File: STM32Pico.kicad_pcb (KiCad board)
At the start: 2 copper layers, 21.1 x 51.3 mm, 25 parts, among them J1 2.54mm header 01x20, J2 2.54mm header 01x20, SW1 Boot Mode, SW2 Reset Switch, U1 STM32F411CEUx, U2 XC6206PxxxMR, X1 ECS-2520MV-xxx-xx

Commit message: worked on the PCB a bit more, added some zones. yet to assign pins to GPIOs
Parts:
- moved R1 40.5 mm to (104.9, 66.9), turned to 90 degrees
- moved C1 30.8 mm to (109.7, 80.1), turned to 180 degrees
- moved C7 28.0 mm to (108.3, 78.5), turned to 270 degrees
- moved C5 26.1 mm to (98.7, 85.2), turned to 45 degrees
- moved C4 22.8 mm to (99.0, 77.9), turned to 270 degrees
- moved R2 19.4 mm to (101.5, 67.4), turned to 90 degrees
- turned D1 to 90 degrees
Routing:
- net D+: track 0.00 -> 11.3 mm, vias 0 -> 2
- net D-: track 0.00 -> 11.1 mm, vias 0 -> 2
- net +3V3: track 2.95 -> 7.47 mm, vias 3 -> 5
- net GND: track 0.00 -> 3.75 mm, vias 0 -> 1
- net Net-(C1-Pad2): track 0.00 -> 2.17 mm
- net Net-(R2-Pad2): track 0.00 -> 2.12 mm
- net Net-(R1-Pad2): track 0.00 -> 1.47 mm
- added copper zone on F.Cu, net +3V3

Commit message: finished up board design, likely needs some check overs and revision.
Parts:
- moved C2 31.4 mm to (105.5, 87.0)
- moved R6 31.1 mm to (101.8, 91.2), turned to 180 degrees
- moved R7 28.8 mm to (97.6, 92.2), turned to 180 degrees
- moved C3 19.0 mm to (100.0, 72.4)
- moved C9 3.70 mm to (103.6, 86.8), turned to 180 degrees
- moved C4 1.38 mm to (100.2, 77.2), turned to 180 degrees
- moved SW2 1.00 mm to (105.5, 90.5)
- moved C1 0.99 mm to (108.7, 80.0)
- moved X1 0.66 mm to (102.3, 89.0)
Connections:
- J1 pad 1: Net-(J1-Pad1) -> PA2
- J1 pad 10: Net-(J1-Pad10) -> PB8
- J1 pad 11: Net-(J1-Pad11) -> PB7
- J1 pad 12: Net-(J1-Pad12) -> PB6
- J1 pad 14: Net-(J1-Pad14) -> PB5
- J1 pad 15: Net-(J1-Pad15) -> PB4
- J1 pad 16: Net-(J1-Pad16) -> PB3
- J1 pad 17: Net-(J1-Pad17) -> PA15
- J1 pad 19: Net-(J1-Pad19) -> PA14
- J1 pad 2: Net-(J1-Pad2) -> PA1
- J1 pad 20: Net-(J1-Pad20) -> PA13
- J1 pad 4: Net-(J1-Pad4) -> PA0
- J1 pad 5: Net-(J1-Pad5) -> PC15
- J1 pad 6: Net-(J1-Pad6) -> PC14
- J1 pad 7: Net-(J1-Pad7) -> PC13
- J1 pad 9: Net-(J1-Pad9) -> PB9
- J2 pad 10: Net-(J2-Pad10) -> PB15
- J2 pad 11: Net-(J2-Pad11) -> PB14
- J2 pad 12: Net-(J2-Pad12) -> PB13
- J2 pad 14: Net-(J2-Pad14) -> PB12
- J2 pad 15: Net-(J2-Pad15) -> PB10
- J2 pad 16: Net-(J2-Pad16) -> PB2
- J2 pad 17: Net-(J2-Pad17) -> PB1
- J2 pad 19: Net-(J2-Pad19) -> PB0
- J2 pad 20: Net-(J2-Pad20) -> PA7
- J2 pad 6: Net-(J2-Pad6) -> PA10
- J2 pad 7: Net-(J2-Pad7) -> PA9
- J2 pad 9: Net-(J2-Pad9) -> PA8
- U1 pad 10: (no net) -> PA0
- U1 pad 11: (no net) -> PA1
- U1 pad 12: (no net) -> PA2
- U1 pad 17: (no net) -> PA7
- U1 pad 18: (no net) -> PB0
- U1 pad 19: (no net) -> PB1
- U1 pad 2: (no net) -> PC13
- U1 pad 20: (no net) -> PB2
- U1 pad 21: (no net) -> PB10
- U1 pad 23: (no net) -> GND
- U1 pad 25: (no net) -> PB12
- U1 pad 26: (no net) -> PB13
- U1 pad 27: (no net) -> PB14
- U1 pad 28: (no net) -> PB15
- U1 pad 29: (no net) -> PA8
- U1 pad 3: (no net) -> PC14
- U1 pad 30: (no net) -> PA9
- U1 pad 31: (no net) -> PA10
- U1 pad 34: (no net) -> PA13
- U1 pad 35: (no net) -> GND
- U1 pad 37: (no net) -> PA14
- U1 pad 38: (no net) -> PA15
- U1 pad 39: (no net) -> PB3
- U1 pad 4: (no net) -> PC15
- U1 pad 40: (no net) -> PB4
- U1 pad 41: (no net) -> PB5
- U1 pad 42: (no net) -> PB6
- U1 pad 43: (no net) -> PB7
- U1 pad 45: (no net) -> PB8
- U1 pad 46: (no net) -> PB9
- U1 pad 47: (no net) -> GND
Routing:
- net +3V3: track 7.47 -> 45.4 mm, vias 5 -> 8
- net PA7: track 0.00 -> 29.6 mm
- net PA2: track 0.00 -> 28.0 mm
- net PA1: track 0.00 -> 25.9 mm
- net PB0: track 0.00 -> 25.4 mm
- net PA13: track 0.00 -> 24.9 mm
- net PA14: track 0.00 -> 21.5 mm
- net PA0: track 0.00 -> 21.4 mm
- net PB1: track 0.00 -> 20.8 mm
- net PB12: track 0.00 -> 20.4 mm
- net PB2: track 0.00 -> 18.7 mm
- net PB10: track 0.00 -> 16.6 mm
- net PB13: track 0.00 -> 16.3 mm
- net PA15: track 0.00 -> 15.9 mm
- net PB14: track 0.00 -> 14.7 mm
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
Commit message: cleaned up some bits and pieces.
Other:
- board text added: "https://github.com/Envious-Data/STM32Pico"

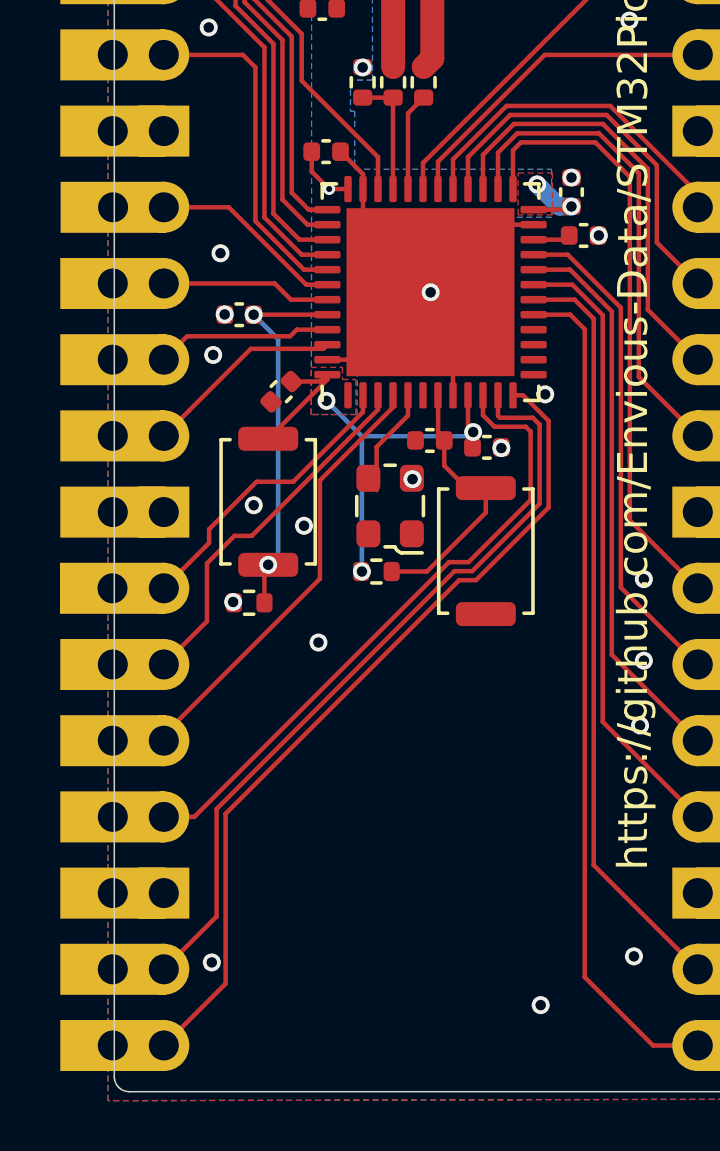
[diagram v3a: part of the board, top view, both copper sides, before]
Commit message: Generated some JLCPCB compatible Gerbers.
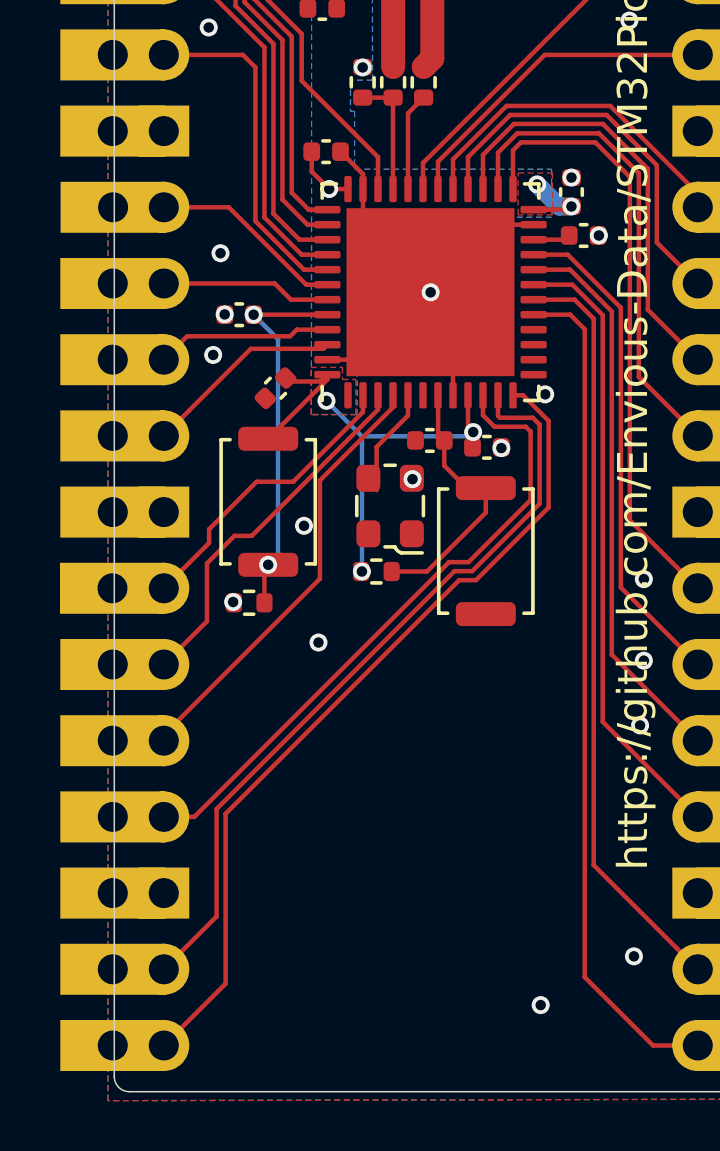
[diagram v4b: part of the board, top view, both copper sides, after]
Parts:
- moved C5 0.22 mm to (98.5, 85.1)
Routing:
- net GND: vias 28 -> 26

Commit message: properly seperated VBUS and VSYS however VSYS is now 5V output only since its not connected to the power management IC
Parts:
- D1: value Schottky 0603 -> 1N4002 0603
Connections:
- D1 pad 1: VBUS -> VSYS
- J2 pad 2: VBUS -> VSYS
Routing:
- added copper zone on F.Cu, net VSYS

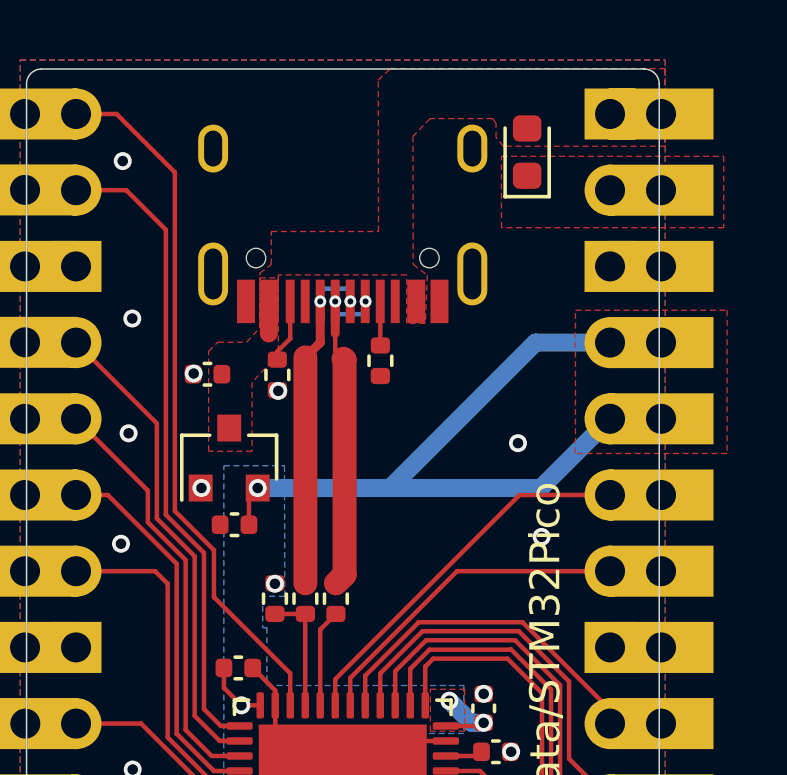
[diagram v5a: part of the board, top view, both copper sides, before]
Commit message: changed my mind - moved power ic to vsys and also adjusted USB traces to correct some phase skew.
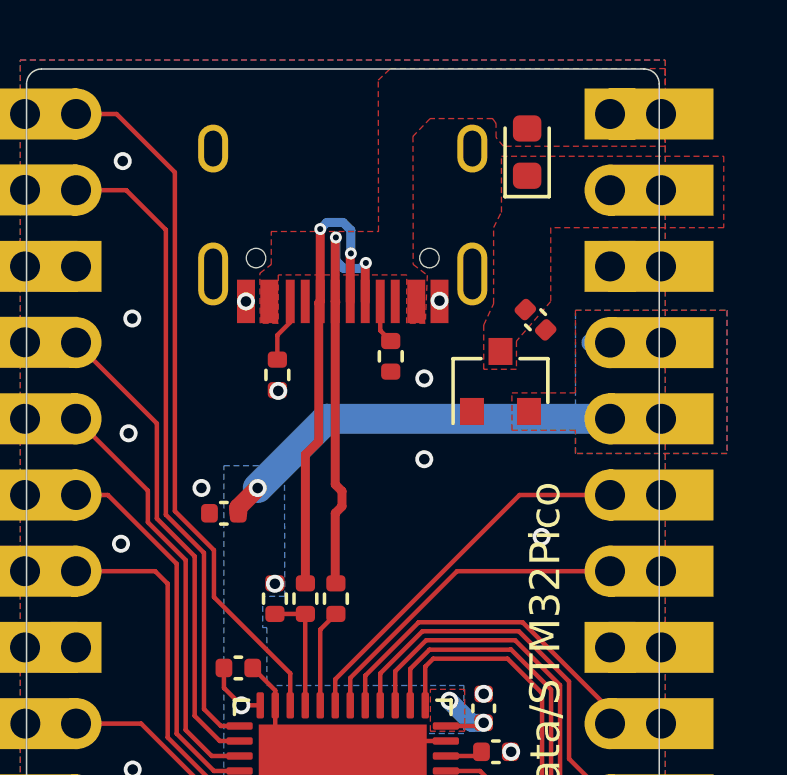
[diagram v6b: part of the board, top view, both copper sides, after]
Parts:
- moved C6 11.1 mm to (110.1, 65.6), turned to 135 degrees
- moved U2 9.40 mm to (108.9, 67.6)
- moved C3 0.52 mm to (99.7, 72.0)
- moved R1 0.38 mm to (105.2, 66.8)
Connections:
- C6 pad 2: VBUS -> VSYS
- U2 pad 3: VBUS -> VSYS
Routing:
- net +3V3: track 45.4 -> 36.5 mm
- net D+: track 11.3 -> 15.6 mm
- net D-: track 11.4 -> 15.0 mm
- net VBUS: track 1.07 -> 0.00 mm
- net GND: vias 26 -> 28
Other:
- net class Default: via_dia 0.6 -> 0.4; via_drill 0.35 -> 0.2
- net class USB_DIFF_90: via_dia 0.6 -> 0.4; via_drill 0.35 -> 0.2
- rule via_min_drill: 0.35 -> 0.2
